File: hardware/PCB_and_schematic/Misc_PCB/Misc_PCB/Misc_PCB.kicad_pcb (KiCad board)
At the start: 2 copper layers, 99.5 x 99.5 mm, 31 parts, among them J1 AC_IN, J2 DC_OUT, J3 LCD_CONN, J6 LCD_DISPLAY, J8 DIODE_BLINK_METER, Q1 IRF540N, Q10 BC817, Q2 IRF540N, Q3 IRF540N, Q4 IRF540N, Q8 BC547, Q9 BC817, U1 LT4320xDD-1, U4 74HC595

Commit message: progress with esp power pcb
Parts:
- added C10: 470u/16V, Capacitor_THT:CP_Radial_D10.0mm_P5.00mm, F.Cu at (176.0, -0.53)
- added C11: 100n, Resistor_SMD:R_0805_2012Metric_Pad1.20x1.40mm_HandSolder, F.Cu at (131.4, -25.0)
- added C14: 100n, Capacitor_SMD:C_0805_2012Metric_Pad1.18x1.45mm_HandSolder, F.Cu at (140.9, 20.9)
- added C4: 100n, Capacitor_SMD:C_0805_2012Metric_Pad1.18x1.45mm_HandSolder, F.Cu at (140.9, 8.87)
- added C5: 470u/40V, Capacitor_THT:CP_Radial_D14.0mm_P5.00mm, F.Cu at (153.7, -14.1)
- added C6: 100n, Resistor_SMD:R_0805_2012Metric_Pad1.20x1.40mm_HandSolder, F.Cu at (131.4, -27.9)
- added C7: 0R, Capacitor_SMD:C_0805_2012Metric_Pad1.18x1.45mm_HandSolder, F.Cu at (140.9, 11.9)
- added C8: 100n, Capacitor_SMD:C_0805_2012Metric_Pad1.18x1.45mm_HandSolder, F.Cu at (140.9, 14.9)
- added C9: 1u/10V, Capacitor_SMD:C_0805_2012Metric_Pad1.18x1.45mm_HandSolder, F.Cu at (140.9, 17.9)
- added D11: LED, LED_THT:LED_D5.0mm, F.Cu at (165.5, -25.6)
- added D12: LED, LED_THT:LED_D5.0mm, F.Cu at (173.0, -25.6)
- added D13: LED, LED_THT:LED_D5.0mm, F.Cu at (180.5, -25.6)
- added D4: D_TVS, Diode_SMD:D_SMC, F.Cu at (165.0, 12.1)
- added D5: D_TVS, Diode_SMD:D_SMC, F.Cu at (165.0, 19.8)
- added D7: 1N4148, Diode_THT:D_DO-35_SOD27_P7.62mm_Horizontal, F.Cu at (165.5, -11.6)
- added D8: LED, LED_THT:LED_D5.0mm, F.Cu at (150.5, -25.6)
- added D9: LED, LED_THT:LED_D5.0mm, F.Cu at (158.0, -25.6)
- added G***: LOGO, graphic:honeybadger2, F.Cu at (230.3, 138.7)
- added J10: BATT, TerminalBlock:TerminalBlock_bornier-2_P5.08mm, F.Cu at (151.2, 7.28)
- added J11: ICP, Connector_PinHeader_2.54mm:PinHeader_1x06_P2.54mm_Vertical, F.Cu at (136.2, 9.69)
- added J12: LCD_DISPLAY, Connector_JST:JST_XA_B05B-XASK-1-A_1x05_P2.50mm_Vertical, F.Cu at (167.5, -17.6)
- added J6: SOLAR_PANEL, TerminalBlock:TerminalBlock_bornier-2_P5.08mm, F.Cu at (151.2, -1.77)
- added J7: RS485, Connector_PinHeader_2.54mm:PinHeader_1x04_P2.54mm_Vertical, F.Cu at (145.7, 9.69)
- added J8: THERMISTOR, Connector_JST:JST_XA_B02B-XASK-1-A_1x02_P2.50mm_Vertical, F.Cu at (174.0, 12.4)
- added J9: THERMISTOR, Connector_JST:JST_XA_B02B-XASK-1-A_1x02_P2.50mm_Vertical, F.Cu at (174.0, 20.9)
- added Q10: BC817, Package_TO_SOT_SMD:SOT-23, F.Cu at (131.4, 5.85)
- added Q11: BC807, Package_TO_SOT_SMD:SOT-23, F.Cu at (131.4, 10.5)
- added Q12: BC807, Package_TO_SOT_SMD:SOT-23, F.Cu at (131.4, 15.1)
- added Q16: BT139-600, Package_TO_SOT_THT:TO-220-3_Vertical, F.Cu at (336.3, 63.6)
- added Q8: BC817, Package_TO_SOT_SMD:SOT-23, F.Cu at (131.4, -3.40)
- added Q9: BC817, Package_TO_SOT_SMD:SOT-23, F.Cu at (131.4, 1.23)
- added R12: 100m, Resistor_SMD:R_0805_2012Metric_Pad1.20x1.40mm_HandSolder, F.Cu at (131.4, -22.0)
- added R13: 100m, Resistor_SMD:R_0805_2012Metric_Pad1.20x1.40mm_HandSolder, F.Cu at (131.4, -19.1)
- added R14: 510R, Resistor_SMD:R_0805_2012Metric_Pad1.20x1.40mm_HandSolder, F.Cu at (131.4, -16.1)
- added R15: 120R, Resistor_SMD:R_0805_2012Metric_Pad1.20x1.40mm_HandSolder, F.Cu at (131.4, -13.2)
- added R16: 510R, Resistor_SMD:R_0805_2012Metric_Pad1.20x1.40mm_HandSolder, F.Cu at (131.4, -10.2)
- added R17: 510R, Resistor_SMD:R_0805_2012Metric_Pad1.20x1.40mm_HandSolder, F.Cu at (131.4, -7.28)
- added R18: 510R, Resistor_SMD:R_0805_2012Metric_Pad1.20x1.40mm_HandSolder, F.Cu at (136.1, -27.9)
- added R19: 10k, Resistor_SMD:R_0805_2012Metric_Pad1.20x1.40mm_HandSolder, F.Cu at (136.1, -25.0)
- added R20: 10k, Resistor_SMD:R_0805_2012Metric_Pad1.20x1.40mm_HandSolder, F.Cu at (136.1, -22.0)
- added R21: 100K, Resistor_SMD:R_0805_2012Metric_Pad1.20x1.40mm_HandSolder, F.Cu at (136.1, -19.1)
- added R22: 100k, Resistor_SMD:R_0805_2012Metric_Pad1.20x1.40mm_HandSolder, F.Cu at (136.1, -16.1)
- added R23: 100k, Resistor_SMD:R_0805_2012Metric_Pad1.20x1.40mm_HandSolder, F.Cu at (136.1, -13.2)
- added R24: 50mR, Resistor_SMD:R_0805_2012Metric_Pad1.20x1.40mm_HandSolder, F.Cu at (136.1, -10.2)
- added R25: 100K, Resistor_SMD:R_0805_2012Metric_Pad1.20x1.40mm_HandSolder, F.Cu at (136.1, -7.28)
- added R26: 100m, Resistor_SMD:R_0805_2012Metric_Pad1.20x1.40mm_HandSolder, F.Cu at (140.9, -27.9)
- added R27: 10k, Resistor_SMD:R_0805_2012Metric_Pad1.20x1.40mm_HandSolder, F.Cu at (140.9, -25.0)
- added R28: 10k, Resistor_SMD:R_0805_2012Metric_Pad1.20x1.40mm_HandSolder, F.Cu at (140.9, -22.0)
- added R29: 10k, Resistor_SMD:R_0805_2012Metric_Pad1.20x1.40mm_HandSolder, F.Cu at (140.9, -19.1)
- added R30: 10K, Resistor_SMD:R_0805_2012Metric_Pad1.20x1.40mm_HandSolder, F.Cu at (140.9, -16.1)
- added R31: 220R, Resistor_SMD:R_0805_2012Metric_Pad1.20x1.40mm_HandSolder, F.Cu at (140.9, -13.2)
- added R32: 10K, Resistor_SMD:R_0805_2012Metric_Pad1.20x1.40mm_HandSolder, F.Cu at (140.9, -10.2)
- added R33: 220R, Resistor_SMD:R_0805_2012Metric_Pad1.20x1.40mm_HandSolder, F.Cu at (140.9, -7.28)
- added R35: 1k, Resistor_SMD:R_0805_2012Metric_Pad1.20x1.40mm_HandSolder, F.Cu at (145.6, -27.9)
- added R38: 10K, Resistor_SMD:R_0805_2012Metric_Pad1.20x1.40mm_HandSolder, F.Cu at (145.6, -25.0)
- added R39: 220R, Resistor_SMD:R_0805_2012Metric_Pad1.20x1.40mm_HandSolder, F.Cu at (145.6, -22.0)
- added R40: 10K, Resistor_SMD:R_0805_2012Metric_Pad1.20x1.40mm_HandSolder, F.Cu at (145.6, -19.1)
- added R41: 220R, Resistor_SMD:R_0805_2012Metric_Pad1.20x1.40mm_HandSolder, F.Cu at (145.6, -16.1)
- added R42: 10K, Resistor_SMD:R_0805_2012Metric_Pad1.20x1.40mm_HandSolder, F.Cu at (145.6, -13.2)
- added R43: 220R, Resistor_SMD:R_0805_2012Metric_Pad1.20x1.40mm_HandSolder, F.Cu at (145.6, -10.2)
- added R52: 200R, Resistor_THT:R_Axial_DIN0204_L3.6mm_D1.6mm_P7.62mm_Horizontal, F.Cu at (323.9, 61.2)
- added R55: 200R, Resistor_THT:R_Axial_DIN0204_L3.6mm_D1.6mm_P7.62mm_Horizontal, F.Cu at (323.9, 64.4)
- added R56: 200R, Resistor_THT:R_Axial_DIN0204_L3.6mm_D1.6mm_P7.62mm_Horizontal, F.Cu at (323.9, 67.5)
- added R57: 200R, Resistor_THT:R_Axial_DIN0204_L3.6mm_D1.6mm_P7.62mm_Horizontal, F.Cu at (323.9, 70.7)
- added R58: 390R, Resistor_THT:R_Axial_DIN0204_L3.6mm_D1.6mm_P7.62mm_Horizontal, F.Cu at (323.9, 73.8)
- added U10: TL431LP, Package_TO_SOT_THT:TO-92_Inline, F.Cu at (176.7, -10.1)
- added U11: ESP-07, RF_Module:ESP-07, F.Cu at (345.9, 48.3)
- added U3: ST485, Package_SO:SOIC-8_3.9x4.9mm_P1.27mm, F.Cu at (138.1, -2.44)
- added U4: INA226, Package_SO:VSSOP-10_3x3mm_P0.5mm, F.Cu at (183.7, 10.5)
- added U5: LT3652EMSE, Package_SO:MSOP-12-1EP_3x4mm_P0.65mm_EP1.65x2.85mm, F.Cu at (183.6, 20.3)
- added U6: LM358, Package_SO:SOIC-8_3.9x4.9mm_P1.27mm, F.Cu at (138.1, 4.13)
- added U7: INA226, Package_SO:VSSOP-10_3x3mm_P0.5mm, F.Cu at (183.7, 15.1)
- added U8: MC34063AP, Package_DIP:DIP-8_W7.62mm, F.Cu at (149.6, 13.9)
- added U9: PIC16F819-IML, Package_SO:SOIC-20W_7.5x12.8mm_P1.27mm, F.Cu at (166.0, 1.00)
- Q3: renamed from Q1; footprint Package_TO_SOT_THT:TO-220-3_Vertical -> My-Footprints:TO-220-3_Vertical-little-bigger pads
- Q4: footprint Package_TO_SOT_THT:TO-220-3_Vertical -> My-Footprints:TO-220-3_Vertical-little-bigger pads
- Q5: renamed from Q2; footprint Package_TO_SOT_THT:TO-220-3_Vertical -> My-Footprints:TO-220-3_Vertical-little-bigger pads
- Q6: renamed from Q3; footprint Package_TO_SOT_THT:TO-220-3_Vertical -> My-Footprints:TO-220-3_Vertical-little-bigger pads
- moved R5 17.8 mm to (213.4, 52.6), turned to 90 degrees
- moved R10 3.70 mm to (221.4, 69.7), turned to -90 degrees
- moved Q7 3.51 mm to (209.4, 49.6), turned to -90 degrees
- moved R11 2.33 mm to (223.9, 65.8), turned to 90 degrees
- moved R8 0.61 mm to (220.9, 52.2)
- moved R7 0.50 mm to (226.1, 52.5)
- moved R9 0.48 mm to (220.9, 49.0)
- moved C3 0.42 mm to (219.7, 63.2)
- moved C2 0.20 mm to (208.3, 59.6)
- moved R6 0.10 mm to (226.1, 49.4)
- renumbered C2 to C1, C1 to C2, D3 to D1, J8 to J1, J1 to J2, J2 to J3, J3 to J4, J6 to J5, Q10 to Q1, Q9 to Q2, Q8 to Q7, R19 to R1, R15 to R10, R3 to R11, R16 to R2, R20 to R3, R18 to R4, R14 to R5, R17 to R6, R13 to R7, R1 to R8, R2 to R9, U4 to U2
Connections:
- U2 pad 1: DB6 -> DB7
- U2 pad 15: DB7 -> BACKLIGHT_DRIVE
- U2 pad 2: DB5 -> DB6
- U2 pad 3: DB4 -> DB5
- U2 pad 4: E1 -> DB4
- U2 pad 7: BACKLIGHT_DRIVE -> E1
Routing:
- net Net-(J5-Pin_17): track 0.00 -> 45.6 mm
- net +5V: track 0.00 -> 40.9 mm
- net E2: track 0.00 -> 26.6 mm, vias 0 -> 1
- net DB7: track 0.00 -> 24.2 mm
- net DB6: track 0.00 -> 18.6 mm
- net DB5: track 0.00 -> 17.7 mm
- net /Shift Register for LCD Display/CLK: track 0.00 -> 17.6 mm, vias 0 -> 1
- net Net-(Q7-C): track 0.00 -> 16.4 mm
- net /Shift Register for LCD Display/LATCH: track 0.00 -> 16.2 mm, vias 0 -> 1
- net Net-(J3-Pin_1): track 28.9 -> 44.9 mm
- net RS: track 0.00 -> 13.0 mm
- net /Shift Register for LCD Display/DATA: track 0.00 -> 12.8 mm, vias 0 -> 1
- net DB4: track 0.00 -> 11.8 mm, vias 0 -> 1
- net E1: track 0.00 -> 10.5 mm
- net BACKLIGHT_DRIVE: track 0.00 -> 9.39 mm
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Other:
- board text added: "+5V GND DATA CLK LATCH"
- board text added: "BC547"

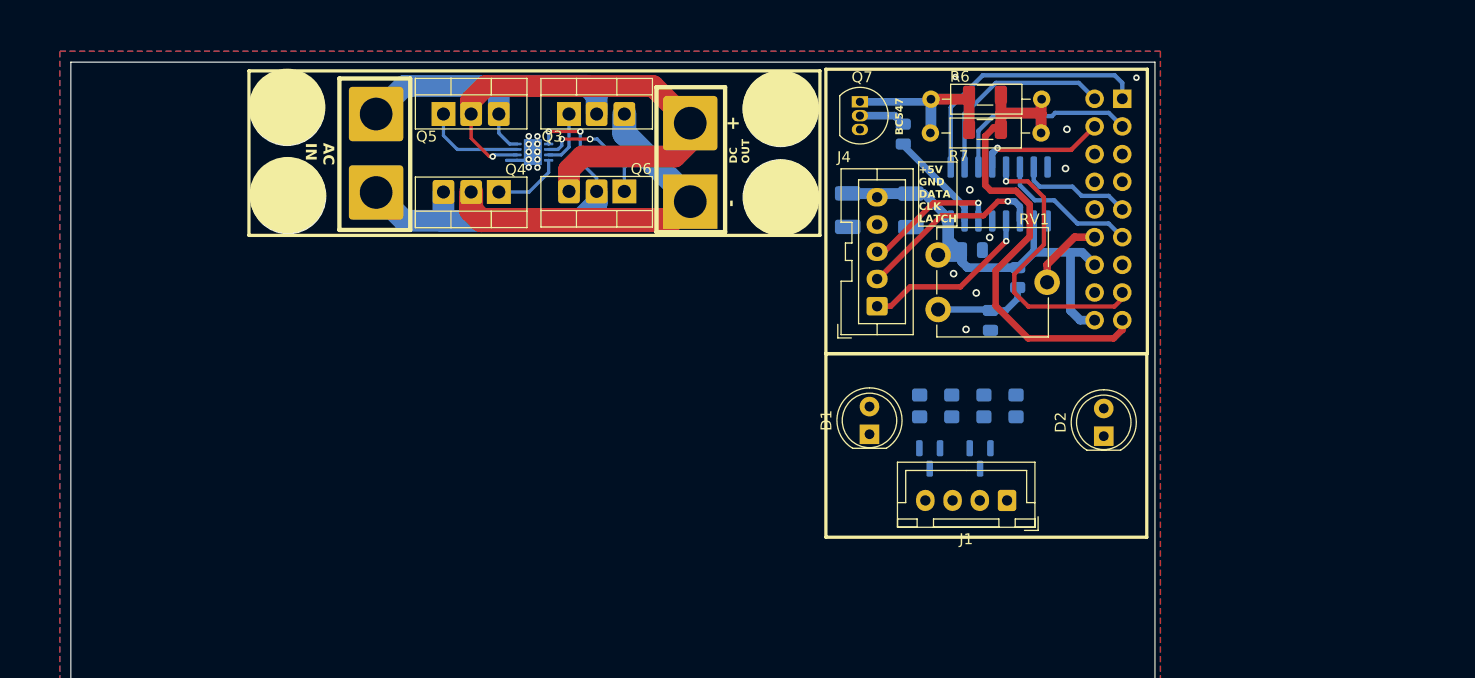
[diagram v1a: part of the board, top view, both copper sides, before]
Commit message: Shift register for LCD update
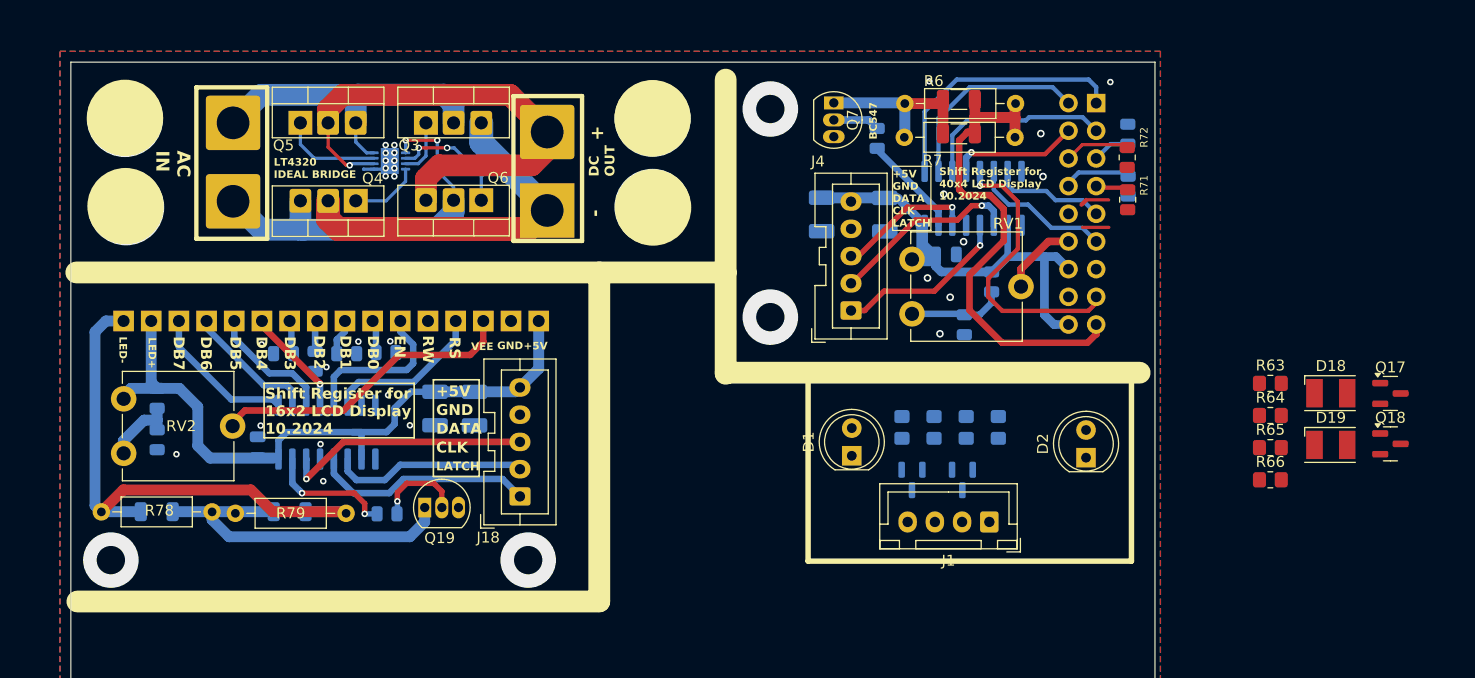
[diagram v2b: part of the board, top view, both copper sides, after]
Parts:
- added C18: 470u/6,3V, Capacitor_Tantalum_SMD:CP_EIA-3528-21_Kemet-B, B.Cu at (170.4, 77.8)
- added C19: 470u/6,3V, Capacitor_Tantalum_SMD:CP_EIA-3528-21_Kemet-B, B.Cu at (174.1, 77.8)
- added C20: 100n, Capacitor_SMD:C_0805_2012Metric, B.Cu at (154.2, 81.3)
- added D18: LED, LED_SMD:LED_PLCC-2_3.4x3.0mm_KA, F.Cu at (252.6, 76.4)
- added D19: LED, LED_SMD:LED_PLCC-2_3.4x3.0mm_KA, F.Cu at (252.6, 81.1)
- added J18: LCD_CONN, Connector_JST:JST_XA_B05B-XASK-1_1x05_P2.50mm_Vertical, F.Cu at (178.2, 85.9)
- added J19: LCD16x2, Connector_PinSocket_2.54mm:PinSocket_1x16_P2.54mm_Vertical, B.Cu at (179.9, 69.8)
- added Q17: BC807, Package_TO_SOT_SMD:SOT-23, F.Cu at (258.1, 76.4)
- added Q18: BC807, Package_TO_SOT_SMD:SOT-23, F.Cu at (258.1, 81.0)
- added Q19: BC547, My-Footprints:TO-92_Inline_LITTLE_BIGGER, F.Cu at (169.8, 86.9)
- added R63: 10K, Resistor_SMD:R_0805_2012Metric_Pad1.20x1.40mm_HandSolder, F.Cu at (247.1, 75.5)
- added R64: 220R, Resistor_SMD:R_0805_2012Metric_Pad1.20x1.40mm_HandSolder, F.Cu at (247.1, 78.4)
- added R65: 10K, Resistor_SMD:R_0805_2012Metric_Pad1.20x1.40mm_HandSolder, F.Cu at (247.1, 81.4)
- added R66: 220R, Resistor_SMD:R_0805_2012Metric_Pad1.20x1.40mm_HandSolder, F.Cu at (247.1, 84.3)
- added R67: 10k, Resistor_SMD:R_0805_2012Metric, B.Cu at (144.9, 76.9)
- added R68: 39k, Resistor_SMD:R_0805_2012Metric, B.Cu at (144.9, 80.7)
- added R69: 10k, Resistor_SMD:R_0805_2012Metric, B.Cu at (166.0, 87.5)
- added R70: 10k, Resistor_SMD:R_0805_2012Metric, B.Cu at (165.9, 72.7)
- added R71: 10k, Resistor_SMD:R_0805_2012Metric, F.Cu at (234.0, 58.6)
- added R72: 10k, Resistor_SMD:R_0805_2012Metric, F.Cu at (234.0, 54.7)
- added R73: 10k, Resistor_SMD:R_0805_2012Metric, B.Cu at (234.0, 52.6)
- added R74: 10k, Resistor_SMD:R_0805_2012Metric, B.Cu at (234.0, 57.4)
- added R75: 10k, Resistor_SMD:R_0805_2012Metric, B.Cu at (162.3, 72.8)
- added R76: 10k, Resistor_SMD:R_0805_2012Metric, B.Cu at (159.4, 73.5)
- added R77: 10k, Resistor_SMD:R_0805_2012Metric, B.Cu at (156.5, 72.8)
- added R78: R, Resistor_THT:R_Axial_DIN0207_L6.3mm_D2.5mm_P10.16mm_Horizontal, F.Cu at (139.8, 87.3)
- added R79: R, Resistor_THT:R_Axial_DIN0207_L6.3mm_D2.5mm_P10.16mm_Horizontal, F.Cu at (162.3, 87.4)
- added R80: R, Resistor_SMD:R_1206_3216Metric, B.Cu at (157.1, 87.3)
- added R81: R, Resistor_SMD:R_1206_3216Metric, B.Cu at (144.9, 87.3)
- added RV2: 10k, Potentiometer_THT:Potentiometer_ACP_CA9-V10_Vertical, F.Cu at (141.8, 81.9)
- added U13: 74HC595, Package_SO:SOIC-16_3.9x9.9mm_P1.27mm, B.Cu at (160.5, 80.0)
- Q7: footprint Package_TO_SOT_THT:TO-92_Inline -> My-Footprints:TO-92_Inline_LITTLE_BIGGER
- moved J2 13.2 mm to (151.9, 58.8)
- moved Q6 13.2 mm to (174.7, 58.7)
- moved J3 13.2 mm to (180.7, 52.4)
- moved Q3 13.2 mm to (169.6, 51.6)
- moved Q4 13.2 mm to (163.2, 58.7)
- moved Q5 13.2 mm to (158.1, 51.6)
- moved U1 13.2 mm to (166.3, 55.1)
- moved J1 2.56 mm to (221.3, 88.2)
- moved R1 2.56 mm to (219.2, 79.5)
- moved R2 2.56 mm to (213.3, 79.5)
- moved R3 2.56 mm to (222.1, 79.5)
- moved R4 2.56 mm to (216.2, 79.5)
- moved D1 2.56 mm to (208.7, 82.1)
- moved D2 2.56 mm to (230.2, 82.3)
- moved Q1 2.56 mm to (218.8, 84.3)
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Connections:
- net /Shift Register for LCD Display/CLK renamed /Shift Register for 40x4 LCD Display/CLK
- net /Shift Register for LCD Display/DATA renamed /Shift Register for 40x4 LCD Display/DATA
- net /Shift Register for LCD Display/LATCH renamed /Shift Register for 40x4 LCD Display/LATCH
- U11 pad 11: unconnected-(U11-GPIO2-Pad11) -> PUSH_BUTTON_1
- U11 pad 14: unconnected-(U11-GPIO5-Pad14) -> DS18B20
- U11 pad 2: unconnected-(U11-ADC-Pad2) -> PUSH_BUTTON_2
- U11 pad 4: unconnected-(U11-GPIO16-Pad4) -> CS
- U11 pad 5: unconnected-(U11-GPIO14-Pad5) -> CLK
- U11 pad 6: unconnected-(U11-GPIO12-Pad6) -> MISO
- U11 pad 7: unconnected-(U11-GPIO13-Pad7) -> MOSI
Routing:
- net +5V: track 40.9 -> 103.2 mm
- net Net-(J19-Pin_16): track 0.00 -> 51.3 mm
- net Net-(Q19-C): track 0.00 -> 32.1 mm
- net Net-(J19-Pin_3): track 0.00 -> 28.0 mm
- net /Shift Register for 16x2 LCD Display/DATA: track 0.00 -> 22.8 mm, vias 0 -> 1
- net /Shift Register for 16x2 LCD Display/LATCH: track 0.00 -> 20.4 mm
- net /Shift Register for 16x2 LCD Display/CLK: track 0.00 -> 18.0 mm
- net RS_A: track 0.00 -> 14.8 mm
- net EN: track 0.00 -> 14.8 mm
- net DB7_A: track 0.00 -> 13.7 mm
- net DB6_A: track 0.00 -> 12.2 mm
- net BACKLIGHT_DRIVE_A: track 0.00 -> 11.7 mm, vias 0 -> 2
- net DB5_A: track 0.00 -> 11.7 mm
- net DB4_A: track 0.00 -> 9.93 mm, vias 0 -> 1
- net Net-(Q19-B): track 0.00 -> 8.09 mm, vias 0 -> 1
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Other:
- board text added: "+5V"
- board text added: "74HC595"
- board text added: "CLK"
- board text added: "DATA"
- board text added: "DB0"
- board text added: "DB1"
- board text added: "DB2"
- board text added: "DB3"
- board text added: "DB4"
- board text added: "DB5"
- board text added: "DB6"
- board text added: "DB7"
- board text added: "EN"
- board text added: "GND"
- board text added: "LATCH"
- board text added: "LED+"
- board text added: "LED-"
- board text added: "LT4320 IDEAL BRIDGE"
- board text added: "RS"
- board text added: "RW"
- board text added: "Shift Register for 16x2 LCD Display 10.2024"
- board text added: "Shift Register for 40x4 LCD Display 10.2024"
- board text added: "VEE"

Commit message: add footprint association
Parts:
- removed U9: PIC16F819-IML, Package_SO:SOIC-20W_7.5x12.8mm_P1.27mm
- added C12: 100n, Capacitor_SMD:C_0805_2012Metric, F.Cu at (68.5, 55.9)
- added C13: 670u/35V, Capacitor_THT:CP_Radial_D10.0mm_P5.00mm, F.Cu at (58.0, 60.2)
- added C15: 100p, Capacitor_SMD:C_0805_2012Metric_Pad1.18x1.45mm_HandSolder, F.Cu at (71.9, 67.5)
- added C16: 560u/6,3V, Capacitor_THT:CP_Radial_D6.3mm_P2.50mm, F.Cu at (64.4, 69.9)
- added C17: 22n/250V AC, Capacitor_THT:C_Rect_L16.5mm_W6.0mm_P15.00mm_MKT, F.Cu at (350.2, 1.31)
- added C21: 470u/6,3V, Capacitor_THT:CP_Radial_D6.3mm_P2.50mm, F.Cu at (201.4, 58.4)
- added C22: 470u/6,3V, Capacitor_SMD:CP_Elec_5x5.7, F.Cu at (169.9, 77.9)
- added D14: 3V3, Diode_SMD:D_MiniMELF, F.Cu at (376.8, 15.2)
- added D15: 3V3, Diode_SMD:D_MiniMELF, F.Cu at (376.8, 18.5)
- added D16: 3V3, Diode_SMD:D_MiniMELF, F.Cu at (376.8, 21.9)
- added D17: 3V3, Diode_SMD:D_MiniMELF, F.Cu at (376.8, 25.2)
- added J14: PROG_INTERFACE, My-Footprints-connectors:Conn-01x06, F.Cu at (350.6, 7.41)
- added J15: DS18B20, Connector_JST:JST_XA_B03B-XASK-1_1x03_P2.50mm_Vertical, F.Cu at (373.5, 9.31)
- added J16: DISPLAY, Connector_JST:JST_XA_B05B-XASK-1_1x05_P2.50mm_Vertical, F.Cu at (356.5, 9.31)
- added L2: 220uH, Inductor_THT:L_Radial_D10.0mm_P5.00mm_Fastron_07P, F.Cu at (9.38, 96.9)
- added Q13: BC817, Package_TO_SOT_SMD:SOT-23_Handsoldering, F.Cu at (370.4, 16.0)
- added Q14: BC817, Package_TO_SOT_SMD:SOT-23_Handsoldering, F.Cu at (370.4, 20.8)
- added Q15: BC817, Package_TO_SOT_SMD:SOT-23_Handsoldering, F.Cu at (370.4, 25.6)
- added R34: 500m, Capacitor_SMD:C_1825_4564Metric, F.Cu at (58.0, 70.2)
- added R36: 10k, Capacitor_SMD:C_0805_2012Metric, F.Cu at (68.5, 58.9)
- added R37: 3k3, Capacitor_SMD:C_0805_2012Metric, F.Cu at (68.5, 62.0)
- added R44: 10k, Capacitor_SMD:C_0805_2012Metric, F.Cu at (377.8, -0.96)
- added R45: 10k, Resistor_SMD:R_0805_2012Metric_Pad1.20x1.40mm_HandSolder, F.Cu at (355.3, 15.0)
- added R46: 10k, Resistor_SMD:R_0805_2012Metric_Pad1.20x1.40mm_HandSolder, F.Cu at (355.3, 18.0)
- added R47: 10k, Resistor_SMD:R_0805_2012Metric_Pad1.20x1.40mm_HandSolder, F.Cu at (355.3, 20.9)
- added R48: 47k, Resistor_SMD:R_0805_2012Metric_Pad1.20x1.40mm_HandSolder, F.Cu at (355.3, 23.9)
- added R49: 47R, Resistor_SMD:R_0805_2012Metric_Pad1.20x1.40mm_HandSolder, F.Cu at (355.3, 26.8)
- added R50: 10k, Resistor_SMD:R_0805_2012Metric_Pad1.20x1.40mm_HandSolder, F.Cu at (360.1, 15.0)
- added R51: 10k, Resistor_SMD:R_0805_2012Metric_Pad1.20x1.40mm_HandSolder, F.Cu at (360.1, 18.0)
- added R53: 560R, Resistor_SMD:R_0805_2012Metric_Pad1.20x1.40mm_HandSolder, F.Cu at (360.1, 20.9)
- added R54: 560R, Resistor_SMD:R_0805_2012Metric_Pad1.20x1.40mm_HandSolder, F.Cu at (360.1, 23.9)
- added R59: 1k, Resistor_SMD:R_0805_2012Metric_Pad1.20x1.40mm_HandSolder, F.Cu at (360.1, 26.8)
- added R60: 1k, Resistor_SMD:R_0805_2012Metric_Pad1.20x1.40mm_HandSolder, F.Cu at (364.8, 15.0)
- added R61: 10k, Resistor_SMD:R_0805_2012Metric_Pad1.20x1.40mm_HandSolder, F.Cu at (364.8, 18.0)
- added R62: 10k, Resistor_SMD:R_0805_2012Metric_Pad1.20x1.40mm_HandSolder, F.Cu at (364.8, 20.9)
- added RV3: S10K275, Varistor:RV_Disc_D7mm_W3.5mm_P5mm, F.Cu at (368.8, -0.59)
- Q16: footprint Package_TO_SOT_THT:TO-220-3_Vertical -> My-Footprints:TO-220-3_V_Wide_Legs
- R24: footprint Resistor_SMD:R_0805_2012Metric_Pad1.20x1.40mm_HandSolder -> Capacitor_SMD:C_1812_4532Metric
- moved U8 153.1 mm to (19.1, 93.9)
- moved C10 147.3 mm to (45.7, 68.2)
- moved C11 147.3 mm to (1.06, 43.8)
- moved C14 147.3 mm to (10.6, 89.7)
- moved C4 147.3 mm to (10.6, 77.6)
- moved C5 147.3 mm to (23.4, 54.7)
- moved C6 147.3 mm to (1.06, 40.9)
- moved C7 147.3 mm to (10.6, 80.7)
- moved C8 147.3 mm to (10.6, 83.7)
- moved C9 147.3 mm to (10.6, 86.7)
- moved D11 147.3 mm to (35.2, 43.1)
- moved D12 147.3 mm to (42.7, 43.1)
- moved D13 147.3 mm to (50.2, 43.1)
- moved D4 147.3 mm to (34.7, 80.8)
- moved D5 147.3 mm to (34.7, 88.6)
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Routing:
- net +5V: track 103.2 -> 107.8 mm, vias 0 -> 2
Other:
- board text added: "DAT"
- board text added: "LAT"
- board text removed: "DATA"
- board text removed: "LATCH"
